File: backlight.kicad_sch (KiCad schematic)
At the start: 105 parts, among them Q1 2N7002, Q2 2N7002, Q3 2N7002

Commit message: Pin wiring
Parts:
- R1, R48, R49, R54: footprint (none) -> Resistor_THT:R_Axial_DIN0204_L3.6mm_D1.6mm_P7.62mm_Horizontal
- R10: renamed from R37; footprint (none) -> Resistor_THT:R_Axial_DIN0204_L3.6mm_D1.6mm_P7.62mm_Horizontal
- R11: renamed from R41; footprint (none) -> Resistor_THT:R_Axial_DIN0204_L3.6mm_D1.6mm_P7.62mm_Horizontal
- R12: renamed from R45; footprint (none) -> Resistor_THT:R_Axial_DIN0204_L3.6mm_D1.6mm_P7.62mm_Horizontal
- R13: renamed from R2; footprint (none) -> Resistor_THT:R_Axial_DIN0204_L3.6mm_D1.6mm_P7.62mm_Horizontal
- R14: renamed from R6; footprint (none) -> Resistor_THT:R_Axial_DIN0204_L3.6mm_D1.6mm_P7.62mm_Horizontal
- R15: renamed from R10; footprint (none) -> Resistor_THT:R_Axial_DIN0204_L3.6mm_D1.6mm_P7.62mm_Horizontal
- R16: renamed from R14; footprint (none) -> Resistor_THT:R_Axial_DIN0204_L3.6mm_D1.6mm_P7.62mm_Horizontal
- R17: renamed from R18; footprint (none) -> Resistor_THT:R_Axial_DIN0204_L3.6mm_D1.6mm_P7.62mm_Horizontal
- R18: renamed from R22; footprint (none) -> Resistor_THT:R_Axial_DIN0204_L3.6mm_D1.6mm_P7.62mm_Horizontal
- R19: renamed from R26; footprint (none) -> Resistor_THT:R_Axial_DIN0204_L3.6mm_D1.6mm_P7.62mm_Horizontal
- R2: renamed from R5; footprint (none) -> Resistor_THT:R_Axial_DIN0204_L3.6mm_D1.6mm_P7.62mm_Horizontal
- R20: renamed from R30; footprint (none) -> Resistor_THT:R_Axial_DIN0204_L3.6mm_D1.6mm_P7.62mm_Horizontal
- R21: renamed from R34; footprint (none) -> Resistor_THT:R_Axial_DIN0204_L3.6mm_D1.6mm_P7.62mm_Horizontal
- R22: renamed from R38; footprint (none) -> Resistor_THT:R_Axial_DIN0204_L3.6mm_D1.6mm_P7.62mm_Horizontal
- R23: renamed from R42; footprint (none) -> Resistor_THT:R_Axial_DIN0204_L3.6mm_D1.6mm_P7.62mm_Horizontal
- R24: renamed from R46; footprint (none) -> Resistor_THT:R_Axial_DIN0204_L3.6mm_D1.6mm_P7.62mm_Horizontal
- R25: renamed from R3; footprint (none) -> Resistor_THT:R_Axial_DIN0204_L3.6mm_D1.6mm_P7.62mm_Horizontal
- R26: renamed from R7; footprint (none) -> Resistor_THT:R_Axial_DIN0204_L3.6mm_D1.6mm_P7.62mm_Horizontal
- R27: renamed from R11; footprint (none) -> Resistor_THT:R_Axial_DIN0204_L3.6mm_D1.6mm_P7.62mm_Horizontal
- R28: renamed from R15; footprint (none) -> Resistor_THT:R_Axial_DIN0204_L3.6mm_D1.6mm_P7.62mm_Horizontal
- R29: renamed from R19; footprint (none) -> Resistor_THT:R_Axial_DIN0204_L3.6mm_D1.6mm_P7.62mm_Horizontal
- R3: renamed from R9; footprint (none) -> Resistor_THT:R_Axial_DIN0204_L3.6mm_D1.6mm_P7.62mm_Horizontal
- R30: renamed from R23; footprint (none) -> Resistor_THT:R_Axial_DIN0204_L3.6mm_D1.6mm_P7.62mm_Horizontal
- R31: renamed from R27; footprint (none) -> Resistor_THT:R_Axial_DIN0204_L3.6mm_D1.6mm_P7.62mm_Horizontal
- R32: renamed from R31; footprint (none) -> Resistor_THT:R_Axial_DIN0204_L3.6mm_D1.6mm_P7.62mm_Horizontal
- R33: renamed from R35; footprint (none) -> Resistor_THT:R_Axial_DIN0204_L3.6mm_D1.6mm_P7.62mm_Horizontal
- R34: renamed from R39; footprint (none) -> Resistor_THT:R_Axial_DIN0204_L3.6mm_D1.6mm_P7.62mm_Horizontal
- R35: renamed from R43; footprint (none) -> Resistor_THT:R_Axial_DIN0204_L3.6mm_D1.6mm_P7.62mm_Horizontal
- R36: renamed from R47; footprint (none) -> Resistor_THT:R_Axial_DIN0204_L3.6mm_D1.6mm_P7.62mm_Horizontal
- R37: renamed from R4; footprint (none) -> Resistor_THT:R_Axial_DIN0204_L3.6mm_D1.6mm_P7.62mm_Horizontal
- R38: renamed from R8; footprint (none) -> Resistor_THT:R_Axial_DIN0204_L3.6mm_D1.6mm_P7.62mm_Horizontal
- R39: renamed from R12; footprint (none) -> Resistor_THT:R_Axial_DIN0204_L3.6mm_D1.6mm_P7.62mm_Horizontal
- R4: renamed from R13; footprint (none) -> Resistor_THT:R_Axial_DIN0204_L3.6mm_D1.6mm_P7.62mm_Horizontal
- R40: renamed from R16; footprint (none) -> Resistor_THT:R_Axial_DIN0204_L3.6mm_D1.6mm_P7.62mm_Horizontal
- R41: renamed from R20; footprint (none) -> Resistor_THT:R_Axial_DIN0204_L3.6mm_D1.6mm_P7.62mm_Horizontal
- R42: renamed from R24; footprint (none) -> Resistor_THT:R_Axial_DIN0204_L3.6mm_D1.6mm_P7.62mm_Horizontal
- R43: renamed from R28; footprint (none) -> Resistor_THT:R_Axial_DIN0204_L3.6mm_D1.6mm_P7.62mm_Horizontal
- R44: renamed from R32; footprint (none) -> Resistor_THT:R_Axial_DIN0204_L3.6mm_D1.6mm_P7.62mm_Horizontal
- R45: renamed from R36; footprint (none) -> Resistor_THT:R_Axial_DIN0204_L3.6mm_D1.6mm_P7.62mm_Horizontal
- R46: renamed from R40; footprint (none) -> Resistor_THT:R_Axial_DIN0204_L3.6mm_D1.6mm_P7.62mm_Horizontal
- R47: renamed from R44; footprint (none) -> Resistor_THT:R_Axial_DIN0204_L3.6mm_D1.6mm_P7.62mm_Horizontal
- R5: renamed from R17; footprint (none) -> Resistor_THT:R_Axial_DIN0204_L3.6mm_D1.6mm_P7.62mm_Horizontal
- R50: renamed from R51; footprint (none) -> Resistor_THT:R_Axial_DIN0204_L3.6mm_D1.6mm_P7.62mm_Horizontal
- R51: renamed from R53; footprint (none) -> Resistor_THT:R_Axial_DIN0204_L3.6mm_D1.6mm_P7.62mm_Horizontal
- R52: renamed from R50; footprint (none) -> Resistor_THT:R_Axial_DIN0204_L3.6mm_D1.6mm_P7.62mm_Horizontal
- R53: renamed from R52; footprint (none) -> Resistor_THT:R_Axial_DIN0204_L3.6mm_D1.6mm_P7.62mm_Horizontal
- R6: renamed from R21; footprint (none) -> Resistor_THT:R_Axial_DIN0204_L3.6mm_D1.6mm_P7.62mm_Horizontal
- R7: renamed from R25; footprint (none) -> Resistor_THT:R_Axial_DIN0204_L3.6mm_D1.6mm_P7.62mm_Horizontal
- R8: renamed from R29; footprint (none) -> Resistor_THT:R_Axial_DIN0204_L3.6mm_D1.6mm_P7.62mm_Horizontal
- R9: renamed from R33; footprint (none) -> Resistor_THT:R_Axial_DIN0204_L3.6mm_D1.6mm_P7.62mm_Horizontal
- renumbered LED37 to LED10, LED41 to LED11, LED45 to LED12, LED2 to LED13, LED6 to LED14, LED10 to LED15, LED14 to LED16, LED18 to LED17, LED22 to LED18, LED26 to LED19, LED5 to LED2, LED30 to LED20, LED34 to LED21, LED38 to LED22, LED42 to LED23, LED46 to LED24, LED3 to LED25, LED7 to LED26, LED11 to LED27, LED15 to LED28, LED19 to LED29, LED9 to LED3, LED23 to LED30, LED27 to LED31, LED31 to LED32, LED35 to LED33, LED39 to LED34, LED43 to LED35, LED47 to LED36, LED4 to LED37, LED8 to LED38, LED12 to LED39, LED13 to LED4, LED16 to LED40, LED20 to LED41, LED24 to LED42, LED28 to LED43, LED32 to LED44, LED36 to LED45, LED40 to LED46, LED44 to LED47, LED17 to LED5, LED21 to LED6, LED25 to LED7, LED29 to LED8, LED33 to LED9

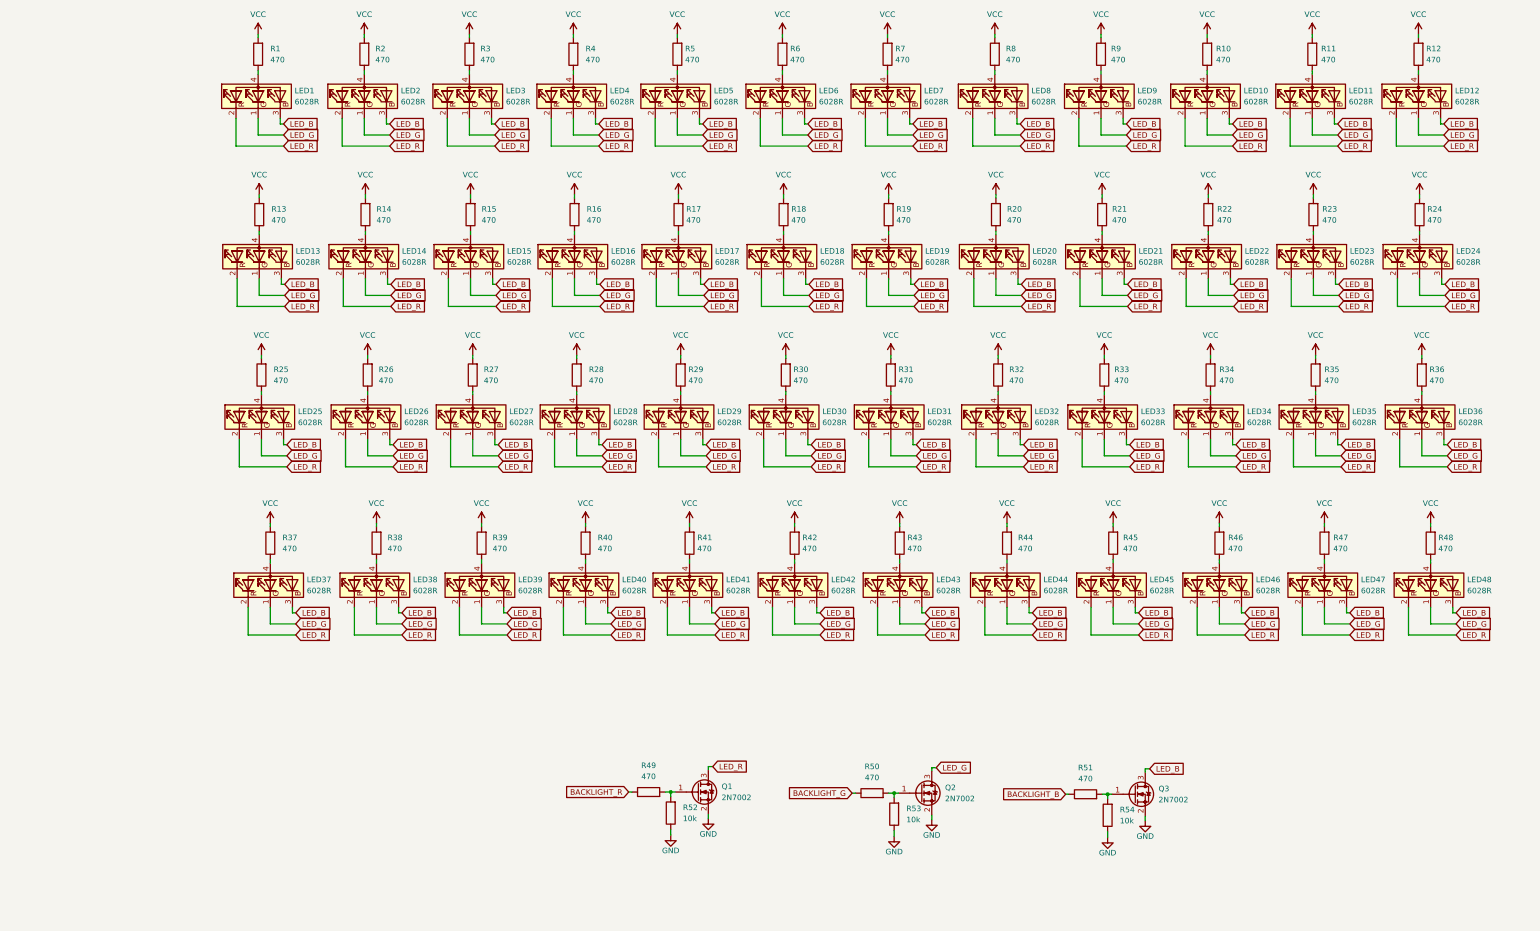
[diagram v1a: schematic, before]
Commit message: Routed components
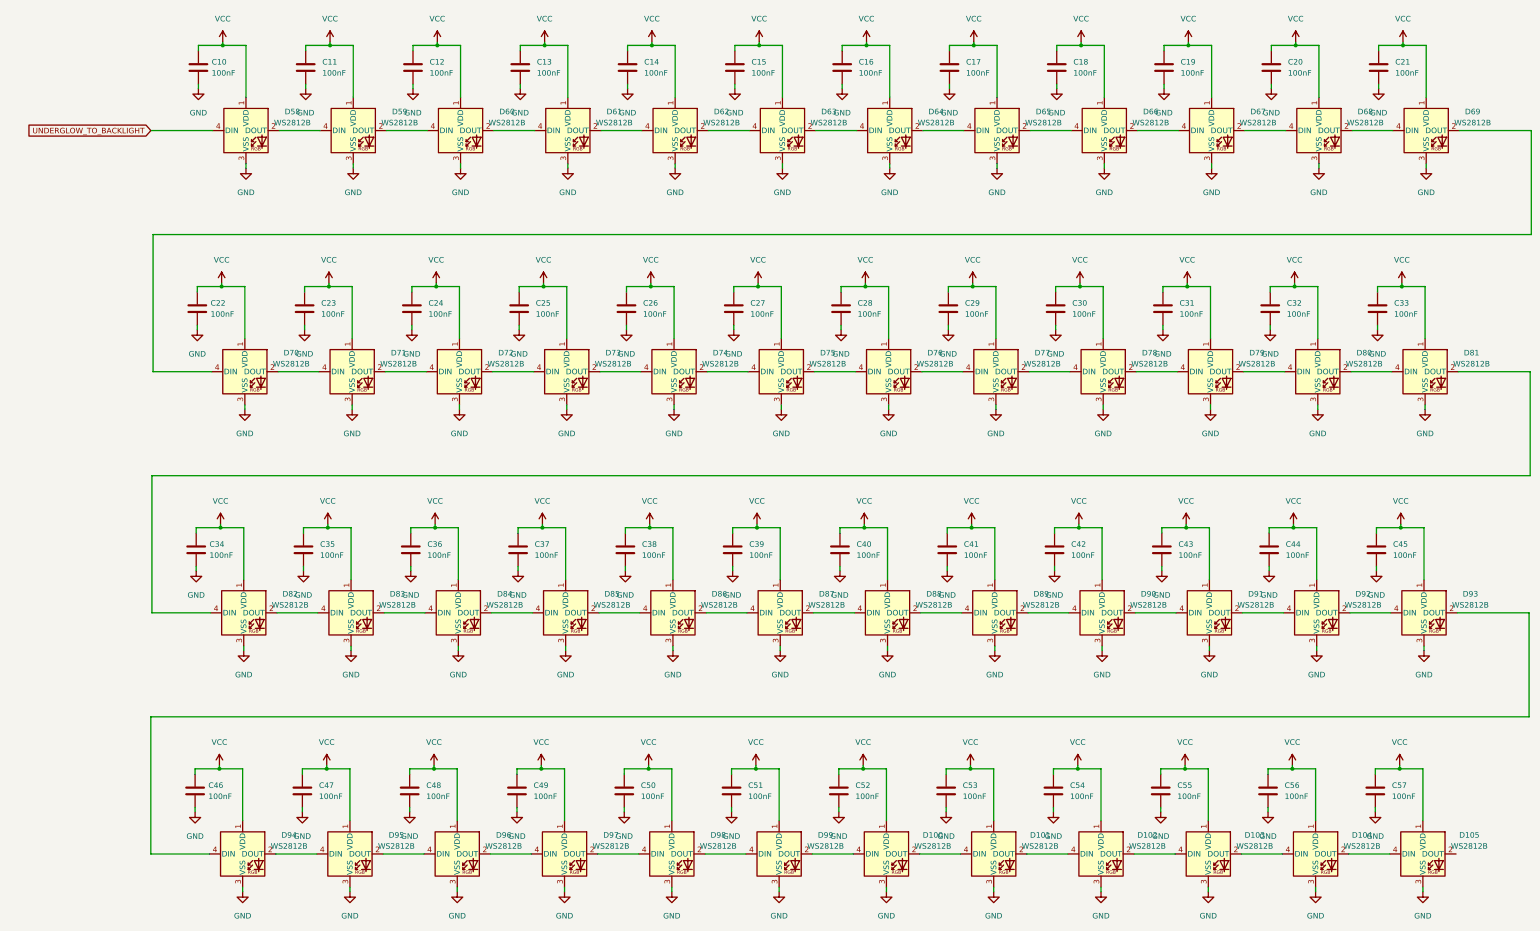
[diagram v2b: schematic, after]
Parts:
- removed LED1, LED10, LED11, LED12, LED13, LED14, LED15, LED16, LED17, LED18, LED19, LED2, LED20, LED21, LED22, LED23, LED24, LED25, LED26, LED27, LED28, LED29, LED3, LED30, LED31, LED32, LED33, LED34, LED35, LED36, LED37, LED38, LED39, LED4, LED40, LED41, LED42, LED43, LED44, LED45, LED46, LED47, LED48, LED5, LED6, LED7, LED8, LED9: 6028R, marbastlib-mx:LED_MX_6028R, symbol marbastlib-various:LED_6028R
- removed Q1, Q2, Q3: 2N7002, Package_TO_SOT_SMD:SOT-23, symbol Transistor_FET:2N7002
- removed R1, R10, R11, R12, R13, R14, R15, R16, R17, R18, R19, R2, R20, R21, R22, R23, R24, R25, R26, R27, R28, R29, R3, R30, R31, R32, R33, R34, R35, R36, R37, R38, R39, R4, R40, R41, R42, R43, R44, R45, R46, R47, R48, R49, R5, R50, R51, R6, R7, R8, R9: 470, Resistor_THT:R_Axial_DIN0204_L3.6mm_D1.6mm_P7.62mm_Horizontal, symbol Device:R
- removed R52, R53, R54: 10k, Resistor_THT:R_Axial_DIN0204_L3.6mm_D1.6mm_P7.62mm_Horizontal, symbol Device:R
- added C10, C11, C12, C13, C14, C15, C16, C17, C18, C19, C20, C21, C22, C23, C24, C25, C26, C27, C28, C29, C30, C31, C32, C33, C34, C35, C36, C37, C38, C39, C40, C41, C42, C43, C44, C45, C46, C47, C48, C49, C50, C51, C52, C53, C54, C55, C56, C57: 100nF, Capacitor_SMD:C_1206_3216Metric_Pad1.33x1.80mm_HandSolder, symbol Device:C
- added D100, D101, D102, D103, D104, D105, D58, D59, D60, D61, D62, D63, D64, D65, D66, D67, D68, D69, D70, D71, D72, D73, D74, D75, D76, D77, D78, D79, D80, D81, D82, D83, D84, D85, D86, D87, D88, D89, D90, D91, D92, D93, D94, D95, D96, D97, D98, D99: WS2812B, marbastlib-mx:LED_MX_6028R, symbol LED:WS2812B
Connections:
- net GND: now also C10.2, C11.2, C12.2, C13.2, C14.2, C15.2, C16.2, C17.2, C18.2, C19.2, C20.2, C21.2, C22.2, C23.2, C24.2, C25.2, C26.2, C27.2, C28.2, C29.2, C30.2, C31.2, C32.2, C33.2, C34.2, C35.2, C36.2, C37.2, C38.2, C39.2, C40.2, C41.2, C42.2, C43.2, C44.2, C45.2, C46.2, C47.2, C48.2, C49.2, C50.2, C51.2, C52.2, C53.2, C54.2, C55.2, C56.2, C57.2, D100.3 (VSS), D101.3 (VSS), D102.3 (VSS), D103.3 (VSS), D104.3 (VSS), D105.3 (VSS), D58.3 (VSS), D59.3 (VSS), D60.3 (VSS), D61.3 (VSS), D62.3 (VSS), D63.3 (VSS), D64.3 (VSS), D65.3 (VSS), D66.3 (VSS), D67.3 (VSS), D68.3 (VSS), D69.3 (VSS), D70.3 (VSS), D71.3 (VSS), D72.3 (VSS), D73.3 (VSS), D74.3 (VSS), D75.3 (VSS), D76.3 (VSS), D77.3 (VSS), D78.3 (VSS), D79.3 (VSS), D80.3 (VSS), D81.3 (VSS), D82.3 (VSS), D83.3 (VSS), D84.3 (VSS), D85.3 (VSS), D86.3 (VSS), D87.3 (VSS), D88.3 (VSS), D89.3 (VSS), D90.3 (VSS), D91.3 (VSS), D92.3 (VSS), D93.3 (VSS), D94.3 (VSS), D95.3 (VSS), D96.3 (VSS), D97.3 (VSS), D98.3 (VSS), D99.3 (VSS)
- net VCC: now also C10.1, C11.1, C12.1, C13.1, C14.1, C15.1, C16.1, C17.1, C18.1, C19.1, C20.1, C21.1, C22.1, C23.1, C24.1, C25.1, C26.1, C27.1, C28.1, C29.1, C30.1, C31.1, C32.1, C33.1, C34.1, C35.1, C36.1, C37.1, C38.1, C39.1, C40.1, C41.1, C42.1, C43.1, C44.1, C45.1, C46.1, C47.1, C48.1, C49.1, C50.1, C51.1, C52.1, C53.1, C54.1, C55.1, C56.1, C57.1, D100.1 (VDD), D101.1 (VDD), D102.1 (VDD), D103.1 (VDD), D104.1 (VDD), D105.1 (VDD), D58.1 (VDD), D59.1 (VDD), D60.1 (VDD), D61.1 (VDD), D62.1 (VDD), D63.1 (VDD), D64.1 (VDD), D65.1 (VDD), D66.1 (VDD), D67.1 (VDD), D68.1 (VDD), D69.1 (VDD), D70.1 (VDD), D71.1 (VDD), D72.1 (VDD), D73.1 (VDD), D74.1 (VDD), D75.1 (VDD), D76.1 (VDD), D77.1 (VDD), D78.1 (VDD), D79.1 (VDD), D80.1 (VDD), D81.1 (VDD), D82.1 (VDD), D83.1 (VDD), D84.1 (VDD), D85.1 (VDD), D86.1 (VDD), D87.1 (VDD), D88.1 (VDD), D89.1 (VDD), D90.1 (VDD), D91.1 (VDD), D92.1 (VDD), D93.1 (VDD), D94.1 (VDD), D95.1 (VDD), D96.1 (VDD), D97.1 (VDD), D98.1 (VDD), D99.1 (VDD)
- new net: D85.2 (DOUT), D86.4 (DIN)
- new net: D84.2 (DOUT), D85.4 (DIN)
- new net: D90.2 (DOUT), D91.4 (DIN)
- new net: D89.2 (DOUT), D90.4 (DIN)
- new net: D78.2 (DOUT), D79.4 (DIN)
- new net: D77.2 (DOUT), D78.4 (DIN)
- new net: D91.2 (DOUT), D92.4 (DIN)
- new net: D70.2 (DOUT), D71.4 (DIN)
- new net: D69.2 (DOUT), D70.4 (DIN)
- new net: D101.2 (DOUT), D102.4 (DIN)
- new net: D100.2 (DOUT), D101.4 (DIN)
- new net: D68.2 (DOUT), D69.4 (DIN)
- new net: D67.2 (DOUT), D68.4 (DIN)
- new net: D83.2 (DOUT), D84.4 (DIN)
- new net: D82.2 (DOUT), D83.4 (DIN)
- new net: D94.2 (DOUT), D95.4 (DIN)
- new net: D93.2 (DOUT), D94.4 (DIN)
- new net: D63.2 (DOUT), D64.4 (DIN)
- new net: D62.2 (DOUT), D63.4 (DIN)
- new net: D97.2 (DOUT), D98.4 (DIN)
- new net: D96.2 (DOUT), D97.4 (DIN)
- new net: D102.2 (DOUT), D103.4 (DIN)
- new net: D80.2 (DOUT), D81.4 (DIN)
- new net: D79.2 (DOUT), D80.4 (DIN)
- new net: D61.2 (DOUT), D62.4 (DIN)
- new net: D60.2 (DOUT), D61.4 (DIN)
- new net: D98.2 (DOUT), D99.4 (DIN)
- new net: D88.2 (DOUT), D89.4 (DIN)
- new net: D87.2 (DOUT), D88.4 (DIN)
- new net: D59.2 (DOUT), D60.4 (DIN)
- new net: D64.2 (DOUT), D65.4 (DIN)
- new net: D86.2 (DOUT), D87.4 (DIN)
- new net: D100.4 (DIN), D99.2 (DOUT)
- new net: D95.2 (DOUT), D96.4 (DIN)
- new net: D104.2 (DOUT), D105.4 (DIN)
- new net: D75.2 (DOUT), D76.4 (DIN)
- new net: D74.2 (DOUT), D75.4 (DIN)
- new net: D92.2 (DOUT), D93.4 (DIN)
- new net: D58.2 (DOUT), D59.4 (DIN)
- new net: D65.2 (DOUT), D66.4 (DIN)
- new net: D81.2 (DOUT), D82.4 (DIN)
- new net: D73.2 (DOUT), D74.4 (DIN)
- new net: D66.2 (DOUT), D67.4 (DIN)
- new net: D103.2 (DOUT), D104.4 (DIN)
- new net: D71.2 (DOUT), D72.4 (DIN)
- new net: D76.2 (DOUT), D77.4 (DIN)
- new net: D72.2 (DOUT), D73.4 (DIN)
- new net UNDERGLOW_TO_BACKLIGHT: D58.4 (DIN)
